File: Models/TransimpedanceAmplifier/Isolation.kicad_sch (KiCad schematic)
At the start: 6 parts

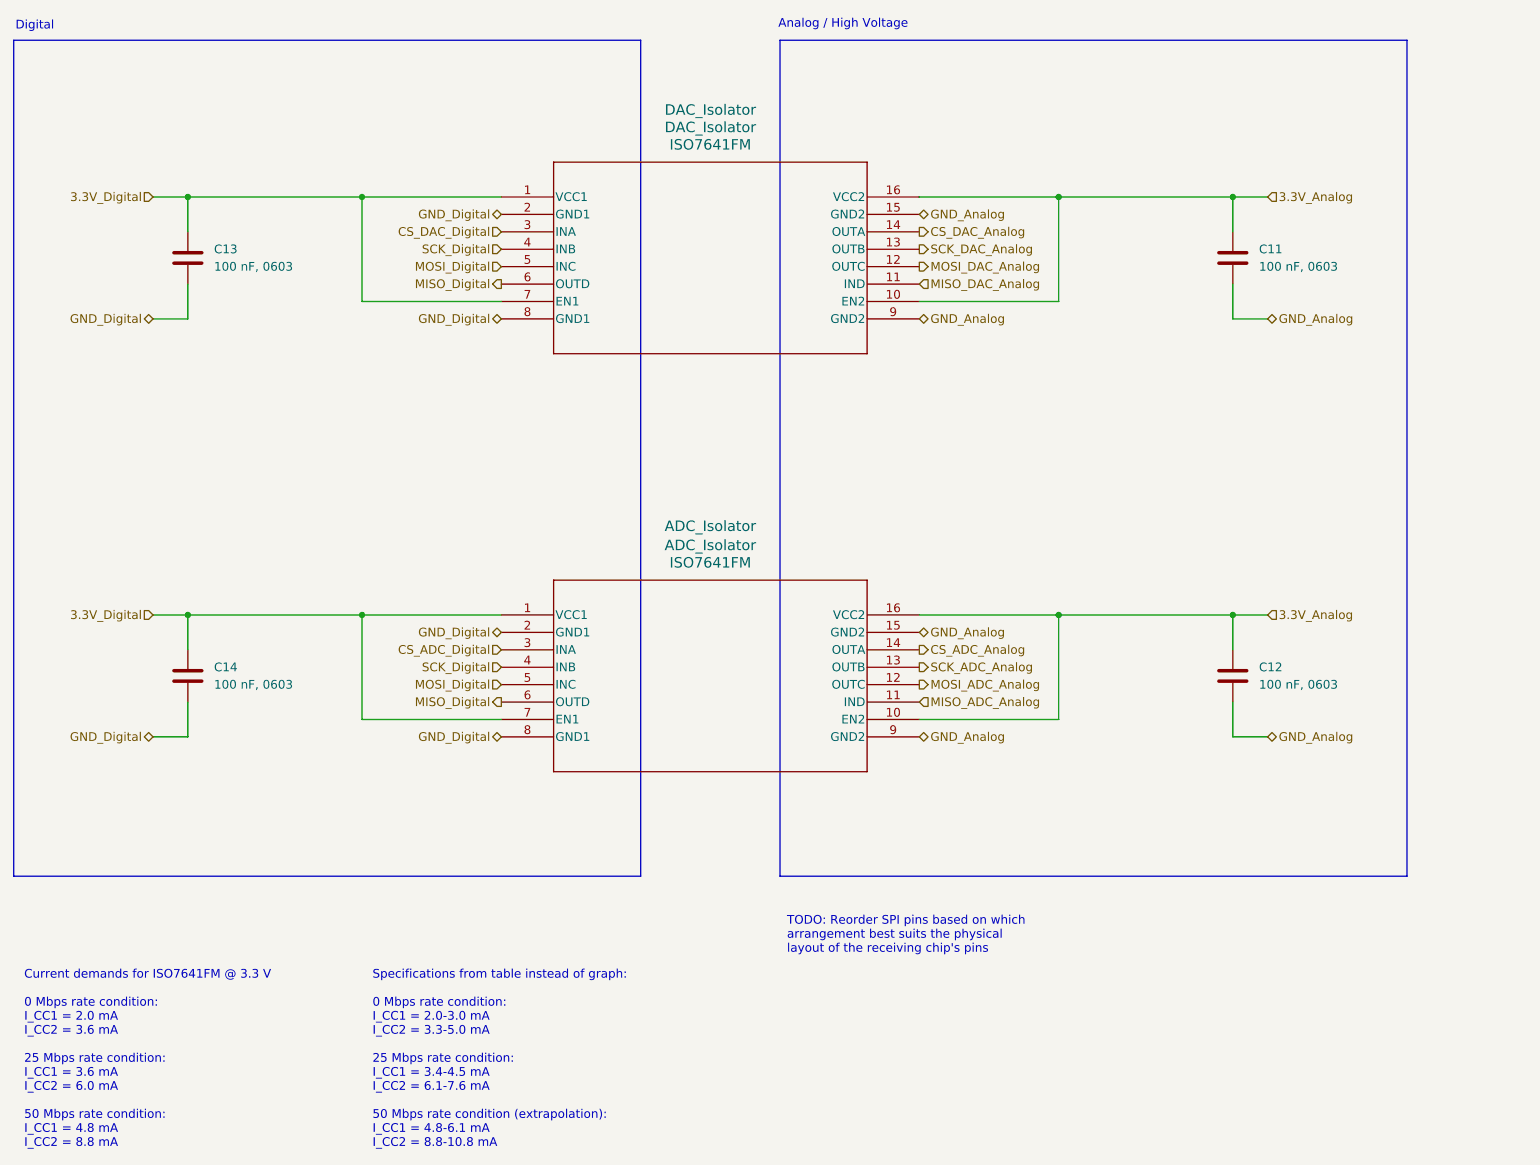
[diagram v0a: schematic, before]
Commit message: Overhauled all of the annotations
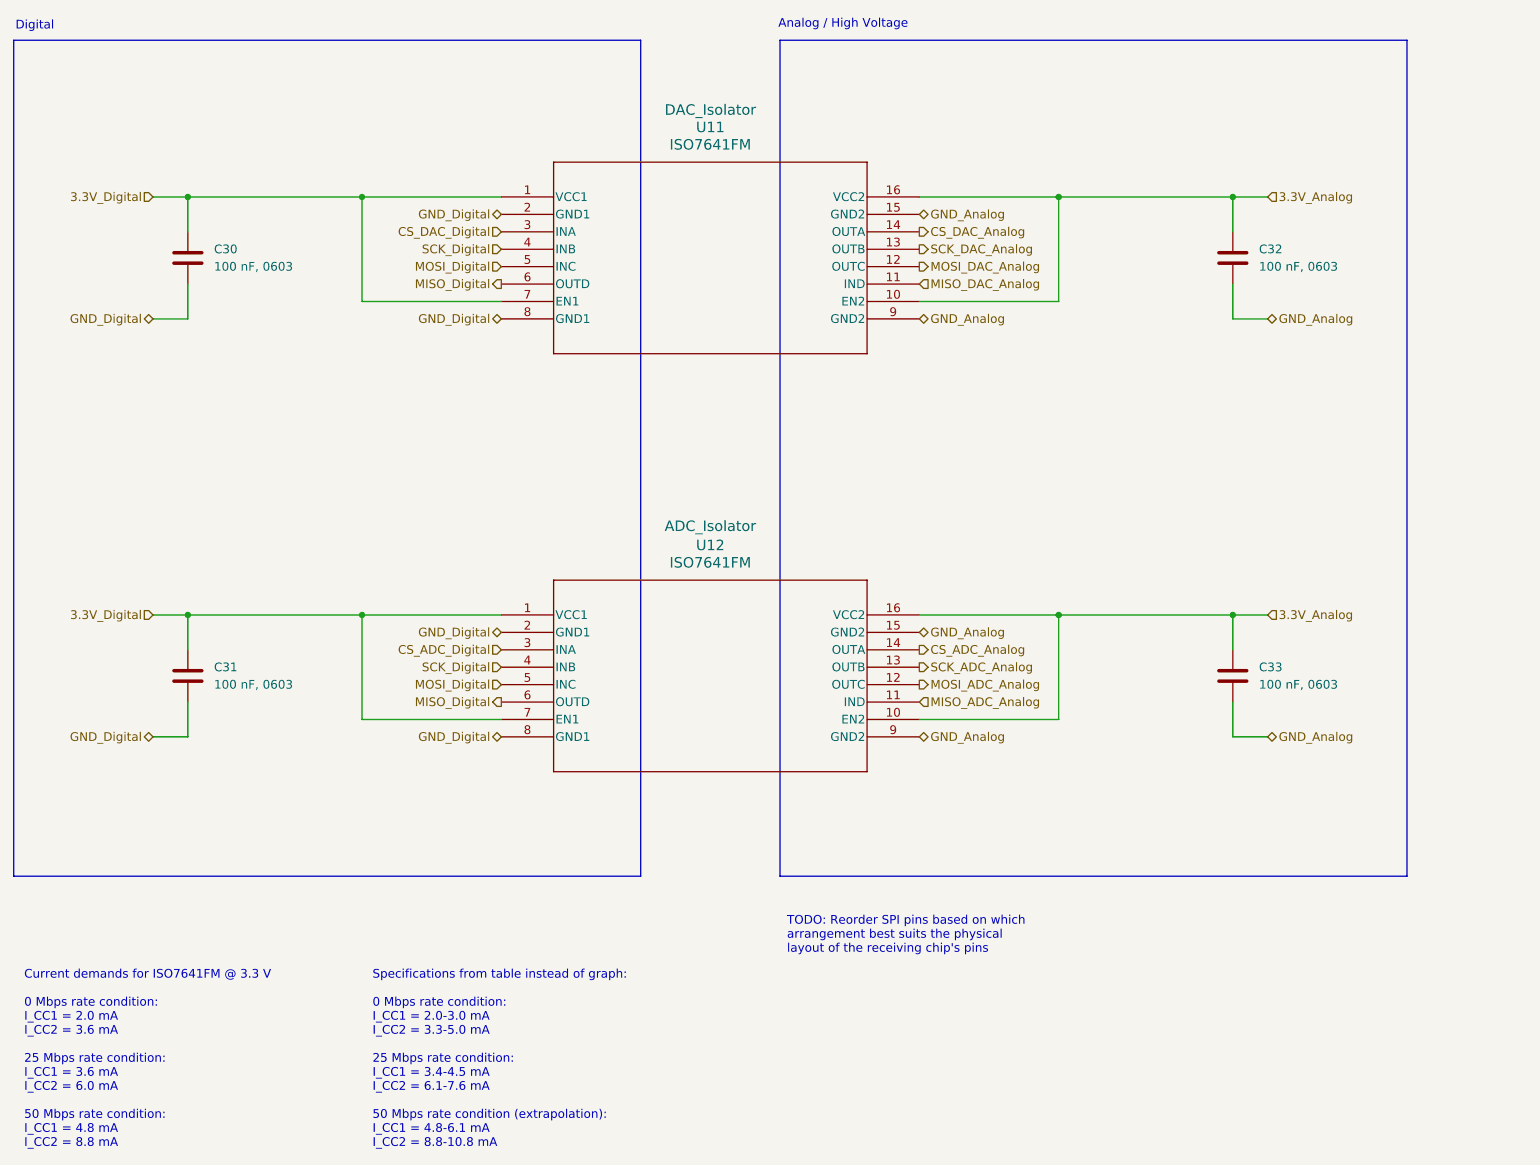
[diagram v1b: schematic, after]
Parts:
- renumbered C13 to C30, C14 to C31, C11 to C32, C12 to C33, DAC_Isolator to U11, ADC_Isolator to U12
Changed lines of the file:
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@@
 		(dnp no)
 		(fields_autoplaced yes)
-		(property "Reference" "C13"
+		(property "Reference" "C30"
 			(at 80.01 53.3399 0)
 			(effects
@@
 			(project "TransimpedanceAmplifier"
 				(path "/ec9f2ae3-e40d-40eb-9760-2b611ee8efd1/7e303428-a18c-4ad4-b002-5ab9c6631588/e0dacc02-a437-4540-b76e-19ca4ea6e74c"
-					(reference "C13")
+					(reference "C30")
 					(unit 1)
 				)
@@
 		(on_board yes)
 		(dnp no)
-		(property "Reference" "ADC_Isolator"
+		(property "Reference" "U12"
 			(at 152.4 96.52 0)
 			(effects
@@
 			(project "TransimpedanceAmplifier"
 				(path "/ec9f2ae3-e40d-40eb-9760-2b611ee8efd1/7e303428-a18c-4ad4-b002-5ab9c6631588/e0dacc02-a437-4540-b76e-19ca4ea6e74c"
-					(reference "ADC_Isolator")
+					(reference "U12")
 					(unit 1)
 				)
@@
 		(dnp no)
 		(fields_autoplaced yes)
-		(property "Reference" "C14"
+		(property "Reference" "C31"
 			(at 80.01 114.2999 0)
 			(effects
@@
 			(project "TransimpedanceAmplifier"
 				(path "/ec9f2ae3-e40d-40eb-9760-2b611ee8efd1/7e303428-a18c-4ad4-b002-5ab9c6631588/e0dacc02-a437-4540-b76e-19ca4ea6e74c"
-					(reference "C14")
+					(reference "C31")
 					(unit 1)
 				)
@@
 		(dnp no)
 		(fields_autoplaced yes)
-		(property "Reference" "C11"
+		(property "Reference" "C32"
 			(at 232.41 53.3399 0)
 			(effects
@@
 			(project ""
 				(path "/ec9f2ae3-e40d-40eb-9760-2b611ee8efd1/7e303428-a18c-4ad4-b002-5ab9c6631588/e0dacc02-a437-4540-b76e-19ca4ea6e74c"
-					(reference "C11")
+					(reference "C32")
 					(unit 1)
 				)
@@
 		(on_board yes)
 		(dnp no)
-		(property "Reference" "DAC_Isolator"
+		(property "Reference" "U11"
 			(at 152.4 35.56 0)
 			(effects
@@
 			(project ""
 				(path "/ec9f2ae3-e40d-40eb-9760-2b611ee8efd1/7e303428-a18c-4ad4-b002-5ab9c6631588/e0dacc02-a437-4540-b76e-19ca4ea6e74c"
-					(reference "DAC_Isolator")
+					(reference "U11")
 					(unit 1)
 				)
@@
 		(dnp no)
 		(fields_autoplaced yes)
-		(property "Reference" "C12"
+		(property "Reference" "C33"
 			(at 232.41 114.2999 0)
 			(effects
@@
 			(project "TransimpedanceAmplifier"
 				(path "/ec9f2ae3-e40d-40eb-9760-2b611ee8efd1/7e303428-a18c-4ad4-b002-5ab9c6631588/e0dacc02-a437-4540-b76e-19ca4ea6e74c"
-					(reference "C12")
-					(unit 1)
-				)
+					(reference "C33")
+					(unit 1)
+				)

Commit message: Every decoupling network now has a dedicated net label
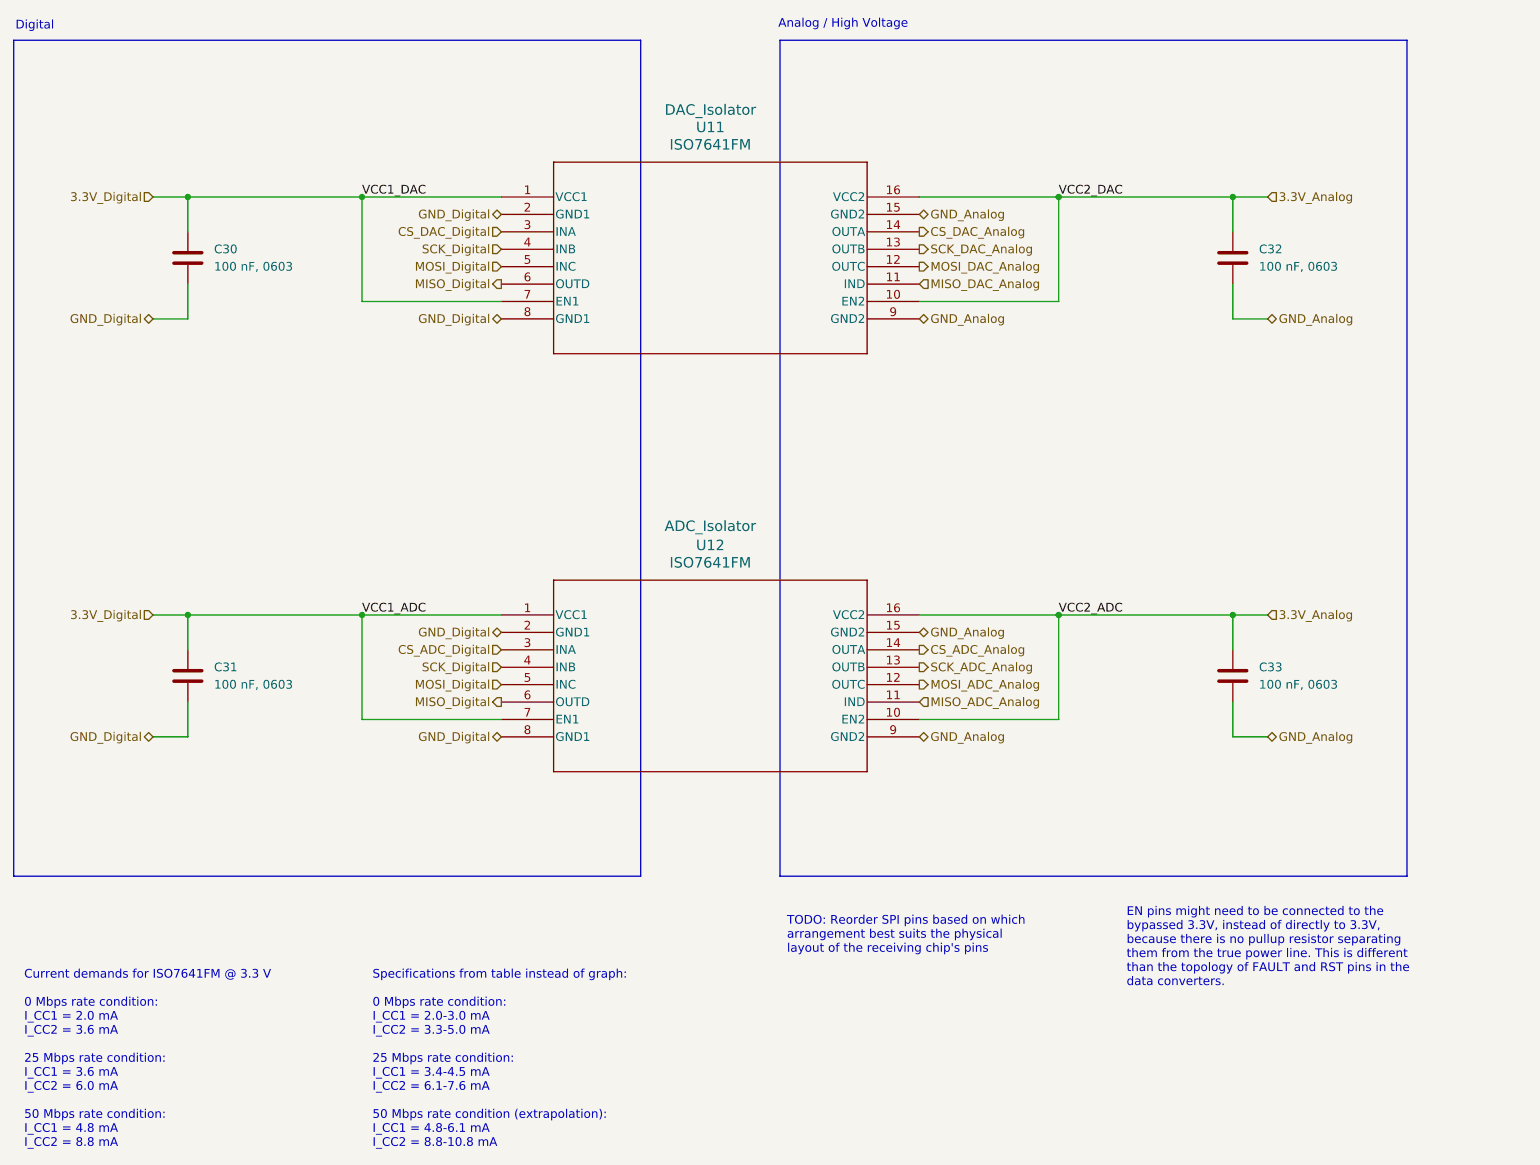
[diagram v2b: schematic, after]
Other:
- note added: "EN pins might need to be connected to the bypassed 3.3V, instead of directly to 3.3V, because there is no pullup resistor separating them from the true power line. This is different than the topology of FAULT and RST pins in the data converters."
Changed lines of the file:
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@@
+		)
+	)
+	(text "EN pins might need to be connected to the\nbypassed 3.3V, instead of directly to 3.3V,\nbecause there is no pullup resistor separating\nthem from the true power line. This is different\nthan the topology of FAULT and RST pins in the\ndata converters."
+		(exclude_from_sim no)
+		(at 213.106 149.352 0)
+		(effects
+			(font
+				(size 1.27 1.27)
+			)
+			(justify left top)
 		)
 	)
@@
 		)
 	)
+	(label "VCC2_DAC"
+		(at 203.2 45.72 0)
+		(effects
+			(font
+				(size 1.27 1.27)
+			)
+			(justify left bottom)
+		)
+	)
+	(label "VCC2_ADC"
+		(at 203.2 106.68 0)
+		(effects
+			(font
+				(size 1.27 1.27)
+			)
+			(justify left bottom)
+		)
+	)
+	(label "VCC1_ADC"
+		(at 101.6 106.68 0)
+		(effects
+			(font
+				(size 1.27 1.27)
+			)
+			(justify left bottom)
+		)
+	)
+	(label "VCC1_DAC"
+		(at 101.6 45.72 0)
+		(effects
+			(font
+				(size 1.27 1.27)
+			)
+			(justify left bottom)
+		)
+	)

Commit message: First successful ERC
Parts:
- added NT5, NT6, NT7, NT8: NetTie_2, symbol Device:NetTie_2
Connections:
- net 3.3V_Analog: now also NT7.2, NT8.2; no longer C32.1, C33.1, U11.10 (EN2), U11.16 (VCC2), U12.10 (EN2), U12.16 (VCC2)
- net 3.3V_Digital: now also NT5.1, NT6.1; no longer C30.1, C31.1, U11.1 (VCC1), U11.7 (EN1), U12.1 (VCC1), U12.7 (EN1)
- new net VCC1_ADC: C31.1, NT6.2, U12.1 (VCC1), U12.7 (EN1)
- new net VCC1_DAC: C30.1, NT5.2, U11.1 (VCC1), U11.7 (EN1)
- new net VCC2_ADC: C33.1, NT8.1, U12.10 (EN2), U12.16 (VCC2)
- new net VCC2_DAC: C32.1, NT7.1, U11.10 (EN2), U11.16 (VCC2)
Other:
- moved on the sheet: C30, C31, C32, C33

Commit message: Finalized the last detail of the schematic
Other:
- note added: "EN pins must connect to the bypassed 3.3V, rather than directly to 3.3V, probably because there is no pullup resistor separating them from the true power line. This is different than the topology of FAULT and RST pins in the data converters."
- note removed: "EN pins might need to be connected to the bypassed 3.3V, instead of directly to 3.3V, because there is no pullup resistor separating them from the true power line. This is different than the topology of FAULT and RST pins in the data converters."
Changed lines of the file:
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@@
 		)
 	)
-	(text "EN pins might need to be connected to the\nbypassed 3.3V, instead of directly to 3.3V,\nbecause there is no pullup resistor separating\nthem from the true power line. This is different\nthan the topology of FAULT and RST pins in the\ndata converters."
+	(text "EN pins must connect to the bypassed 3.3V,\nrather than directly to 3.3V, probably\nbecause there is no pullup resistor separating\nthem from the true power line. This is different\nthan the topology of FAULT and RST pins in the\ndata converters."
 		(exclude_from_sim no)
 		(at 213.106 149.352 0)

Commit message: Working on filling in the last details of the schematics
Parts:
- C30, C31, C32, C33: footprint (none) -> TwoTerminal:CAPC0603; Cost (none) -> $0.00; RoHS Compliant (none) -> NO
- NT5, NT6, NT7, NT8, U11, U12: Cost (none) -> $0.00; RoHS Compliant (none) -> NO
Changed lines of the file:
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@@
+			)
+		)
+		(property "Cost" "$0.00"
+			(at 226.06 45.72 0)
+			(effects
+				(font
+					(size 1.27 1.27)
+				)
+				(hide yes)
+			)
+		)
+		(property "RoHS Compliant" "NO"
+			(at 226.06 45.72 0)
+			(effects
+				(font
+					(size 1.27 1.27)
+				)
+				(hide yes)
 			)
 		)
@@
 			)
 		)
-		(property "Footprint" ""
+		(property "Footprint" "TwoTerminal:CAPC0603"
 			(at 85.3948 58.42 0)
 			(effects
@@
 		)
 		(property "Purchase Link" "https://www.digikey.com/en/products/detail/murata-electronics/GRM188R72A104KA35D/702549"
+			(at 86.36 54.61 0)
+			(effects
+				(font
+					(size 1.27 1.27)
+				)
+				(hide yes)
+			)
+		)
+		(property "Cost" "$0.00"
+			(at 86.36 54.61 0)
+			(effects
+				(font
+					(size 1.27 1.27)
+				)
+				(hide yes)
+			)
+		)
+		(property "RoHS Compliant" "NO"
 			(at 86.36 54.61 0)
 			(effects
@@
 		)
 		(property "Purchase Link" "https://www.digikey.com/en/products/detail/texas-instruments/ISO7641FMDWR/2799299"
+			(at 121.92 106.68 0)
+			(effects
+				(font
+					(size 1.27 1.27)
+				)
+				(hide yes)
+			)
+		)
+		(property "Cost" "$0.00"
+			(at 121.92 106.68 0)
+			(effects
+				(font
+					(size 1.27 1.27)
+				)
+				(hide yes)
+			)
+		)
+		(property "RoHS Compliant" "NO"
 			(at 121.92 106.68 0)
 			(effects
@@
 			)
 		)
-		(property "Footprint" ""
+		(property "Footprint" "TwoTerminal:CAPC0603"
 			(at 85.3948 119.38 0)
 			(effects
@@
 		)
 		(property "Purchase Link" "https://www.digikey.com/en/products/detail/murata-electronics/GRM188R72A104KA35D/702549"
+			(at 86.36 115.57 0)
+			(effects
+				(font
+					(size 1.27 1.27)
+				)
+				(hide yes)
+			)
+		)
+		(property "Cost" "$0.00"
+			(at 86.36 115.57 0)
+			(effects
+				(font
+					(size 1.27 1.27)
+				)
+				(hide yes)
+			)
+		)
+		(property "RoHS Compliant" "NO"
 			(at 86.36 115.57 0)
 			(effects
@@
 			)
 		)
-		(property "Footprint" ""
+		(property "Footprint" "TwoTerminal:CAPC0603"
 			(at 219.4052 58.42 0)
 			(effects
@@
 		)
 		(property "Purchase Link" "https://www.digikey.com/en/products/detail/murata-electronics/GRM188R72A104KA35D/702549"
+			(at 218.44 54.61 0)
+			(effects
+				(font
+					(size 1.27 1.27)
+				)
+				(hide yes)
+			)
+		)
+		(property "Cost" "$0.00"
+			(at 218.44 54.61 0)
+			(effects
+				(font
+					(size 1.27 1.27)
+				)
+				(hide yes)
+			)
+		)
+		(property "RoHS Compliant" "NO"
 			(at 218.44 54.61 0)
 			(effects
@@
 			)
 		)
+		(property "Cost" "$0.00"
+			(at 226.06 106.68 0)
+			(effects
+				(font
+					(size 1.27 1.27)
+				)
+				(hide yes)
+			)
+		)
+		(property "RoHS Compliant" "NO"
+			(at 226.06 106.68 0)
+			(effects
+				(font
+					(size 1.27 1.27)
+				)
+				(hide yes)
+			)
+		)
 		(pin "1"
 		)
@@
 		)
 		(property "Purchase Link" "https://www.digikey.com/en/products/detail/texas-instruments/ISO7641FMDWR/2799299"
+			(at 121.92 45.72 0)
+			(effects
+				(font
+					(size 1.27 1.27)
+				)
+				(hide yes)
+			)
+		)
+		(property "Cost" "$0.00"
+			(at 121.92 45.72 0)
+			(effects
+				(font
+					(size 1.27 1.27)
+				)
+				(hide yes)
+			)
+		)
+		(property "RoHS Compliant" "NO"
 			(at 121.92 45.72 0)
 			(effects
@@
 			)
 		)
+		(property "Cost" "$0.00"
+			(at 78.74 106.68 0)
+			(effects
+				(font
+					(size 1.27 1.27)
+				)
+				(hide yes)
+			)
+		)
+		(property "RoHS Compliant" "NO"
+			(at 78.74 106.68 0)
+			(effects
+				(font
+					(size 1.27 1.27)
+				)
+				(hide yes)
+			)
+		)
 		(pin "1"
 		)
@@
 			)
 		)
+		(property "Cost" "$0.00"
+			(at 78.74 45.72 0)
+			(effects
+				(font
+					(size 1.27 1.27)
+				)
+				(hide yes)
+			)
+		)
+		(property "RoHS Compliant" "NO"
+			(at 78.74 45.72 0)
+			(effects
+				(font
+					(size 1.27 1.27)
+				)
+				(hide yes)
+			)
+		)
 		(pin "2"
 		)
@@
 			)
 		)
-		(property "Footprint" ""
+		(property "Footprint" "TwoTerminal:CAPC0603"
 			(at 219.4052 119.38 0)
 			(effects
@@
 			(at 218.44 115.57 0)
 			(effects
+				(font
+					(size 1.27 1.27)
+				)
+				(hide yes)
+			)
+		)
+		(property "Cost" "$0.00"
+			(at 218.44 115.57 0)
+			(effects
+				(font
+					(size 1.27 1.27)
+				)
+				(hide yes)
+			)
+		)
+		(property "RoHS Compliant" "NO"
+			(at 218.44 115.57 0)
+			(effects

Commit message: Fixed a bug in footprint assignment
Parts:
- NT5, NT6, NT7, NT8: footprint (none) -> Connector_Custom:NetTie_0.2mm
- U11, U12: footprint (none) -> IC:ISO7641FM
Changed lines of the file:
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@@
 			)
 		)
-		(property "Footprint" ""
+		(property "Footprint" "Connector_Custom:NetTie_0.2mm"
 			(at 226.06 45.72 0)
 			(effects
@@
 			)
 		)
-		(property "Footprint" ""
+		(property "Footprint" "IC:ISO7641FM"
 			(at 121.92 106.68 0)
 			(effects
@@
 			)
 		)
-		(property "Footprint" ""
+		(property "Footprint" "Connector_Custom:NetTie_0.2mm"
 			(at 226.06 106.68 0)
 			(effects
@@
 			)
 		)
-		(property "Footprint" ""
+		(property "Footprint" "IC:ISO7641FM"
 			(at 121.92 45.72 0)
 			(effects
@@
 			)
 		)
-		(property "Footprint" ""
+		(property "Footprint" "Connector_Custom:NetTie_0.2mm"
 			(at 78.74 106.68 0)
 			(effects
@@
 			)
 		)
-		(property "Footprint" ""
+		(property "Footprint" "Connector_Custom:NetTie_0.2mm"
 			(at 78.74 45.72 0)
 			(effects
